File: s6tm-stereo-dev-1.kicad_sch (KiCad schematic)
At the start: 61 parts, among them J10 Conn_01x04_Pin, J3 USB_C_Receptacle_USB2.0_14P, SW1 SW_SPDT, SW10 SW_Push, SW2 RotaryEncoder_Switch, SW5 SW_Push, SW6 SW_Push, SW7 SW_Push, SW9 SW_Push, U10 HS96L03W2C03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

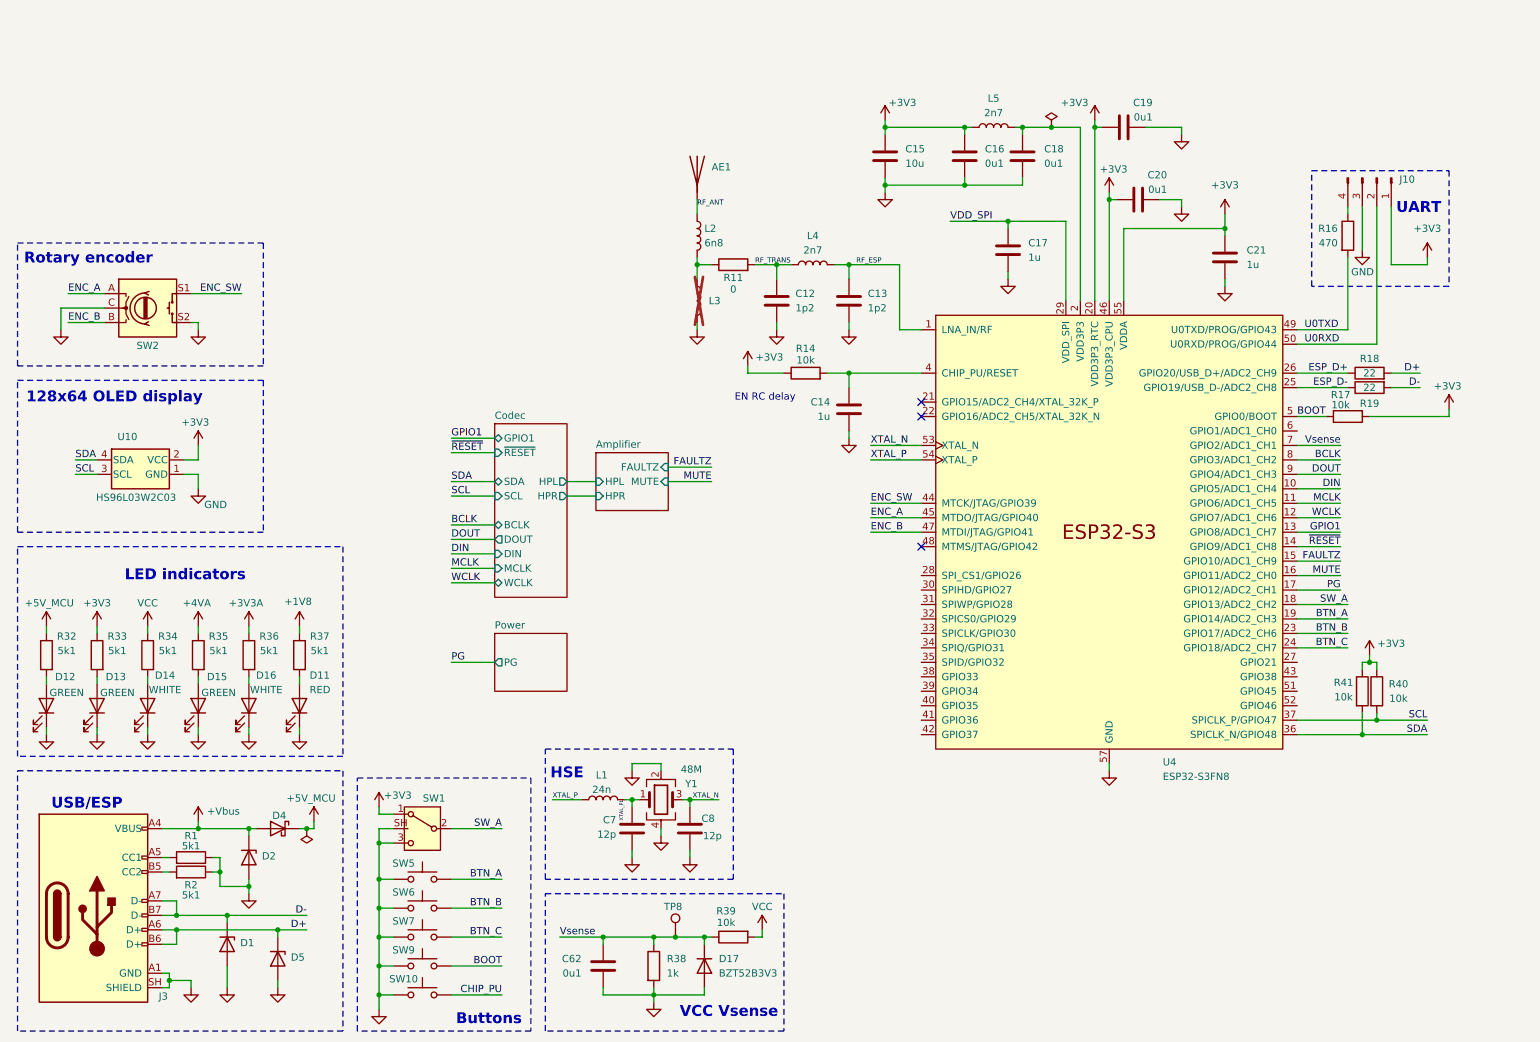
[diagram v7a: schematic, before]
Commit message: schem: add sd card slot
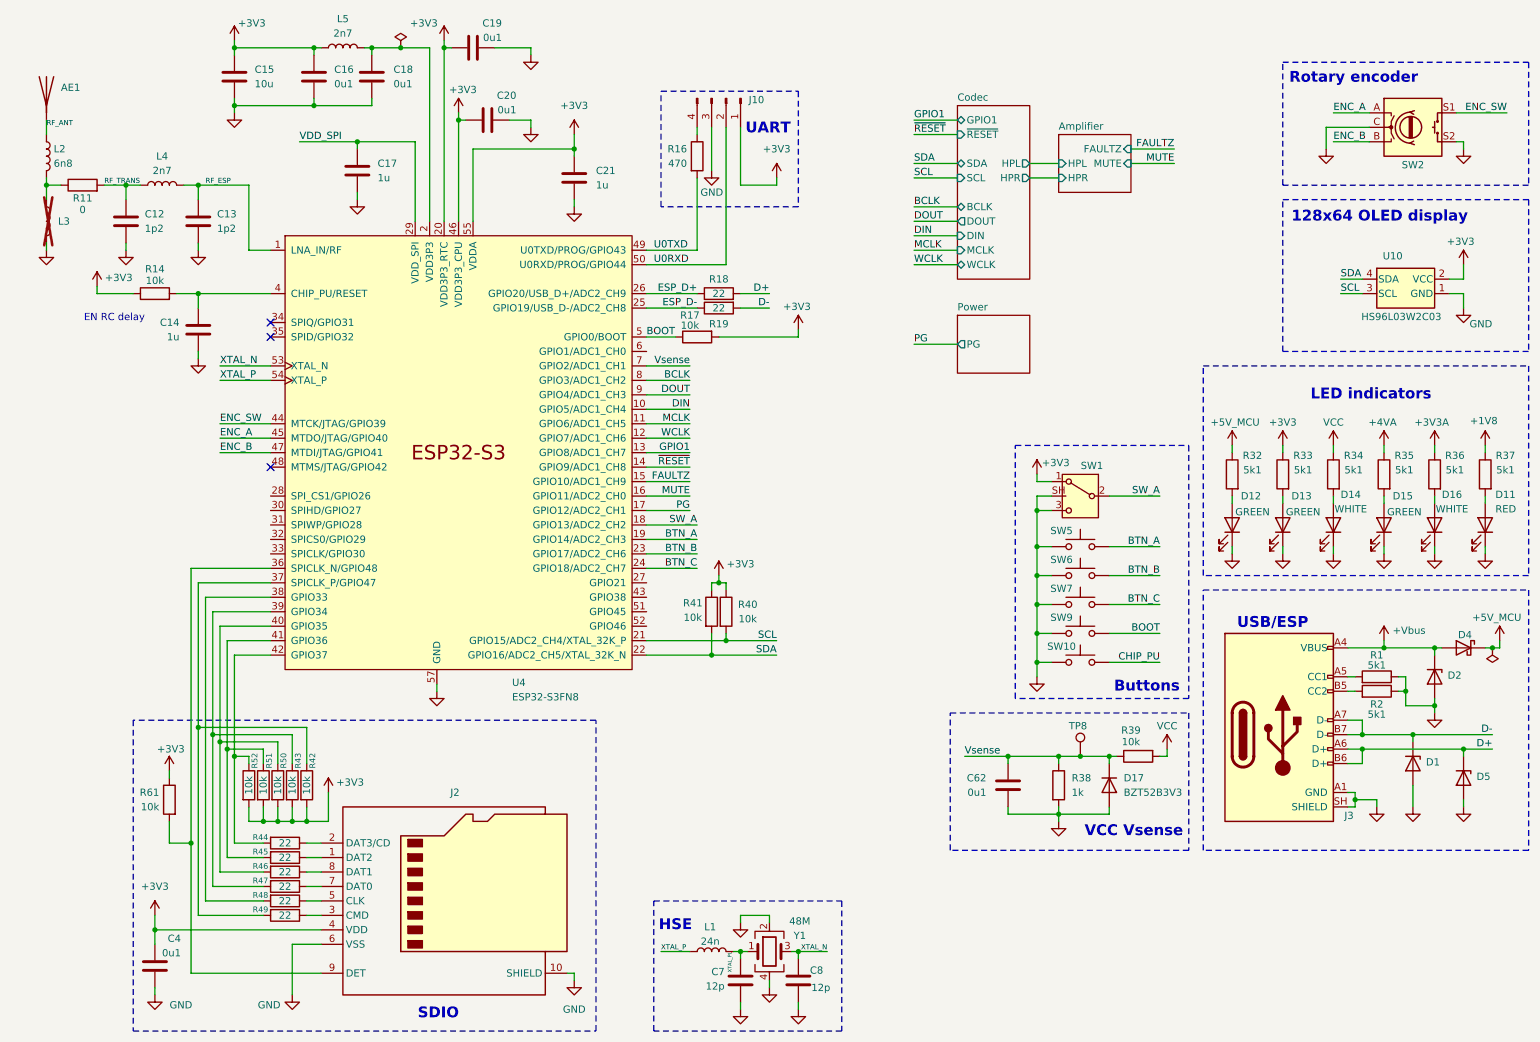
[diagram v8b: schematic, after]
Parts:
- added C4: 0u1, Capacitor_SMD:C_0603_1608Metric, symbol Device:C
- added J2: Micro_SD_Card_Det1, Pers:microSD_Hanbo_TF012, symbol Connector:Micro_SD_Card_Det1
- added R42, R43, R50, R51, R52: 10k, Resistor_SMD:R_0402_1005Metric, symbol Device:R
- added R44, R45, R46, R47, R48, R49: 22, Resistor_SMD:R_0402_1005Metric, symbol Device:R
- added R61: 10k, Resistor_SMD:R_0603_1608Metric, symbol Device:R
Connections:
- net +3V3: now also C4.1, J2.4 (VDD), R42.2, R43.2, R50.2, R51.2, R52.2, R61.1
- net GND: now also C4.2, J2.10 (SHIELD), J2.6 (VSS)
- net SCL: now also U4.21 (GPIO15/ADC2_CH4/XTAL_32K_P); no longer U4.37 (SPICLK_P/GPIO47)
- net SDA: now also U4.22 (GPIO16/ADC2_CH5/XTAL_32K_N); no longer U4.36 (SPICLK_N/GPIO48)
- net at U4.38 (GPIO33): now also R48.2
- net at U4.39 (GPIO34): now also R43.1, R47.2
- net at U4.40 (GPIO35): now also R46.2, R50.1
- net at U4.41 (GPIO36): now also R45.2, R51.1
- net at U4.42 (GPIO37): now also R44.2, R52.1
- new net: J2.1 (DAT2), R45.1
- new net: J2.2 (DAT3/CD), R44.1
- new net: J2.3 (CMD), R49.1
- new net: J2.5 (CLK), R48.1
- new net: J2.7 (DAT0), R47.1
- new net: J2.8 (DAT1), R46.1
- new net: J2.9 (DET), R61.2, U4.36 (SPICLK_N/GPIO48)
- new net: R42.1, R49.2, U4.37 (SPICLK_P/GPIO47)
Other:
- note added: "SDIO"
- moved on the sheet: AE1, C12, C13, C14, C15, C16, C17, C18, C19, C20, C21, C62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
